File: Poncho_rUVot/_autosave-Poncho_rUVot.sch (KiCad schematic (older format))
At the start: 20 parts, among them J1 Screw_Terminal_01x03, K1 G5V-1, P10 Conn_01x04, P11 Conn_01x08, P3 Conn_01x03, P4 Conn_01x03, P5 Conn_01x04, P6 Conn_01x02, P7 Conn_01x02, P8 Conn_01x03, P9 Conn_01x06, Q1 BC548, Q2 BC548

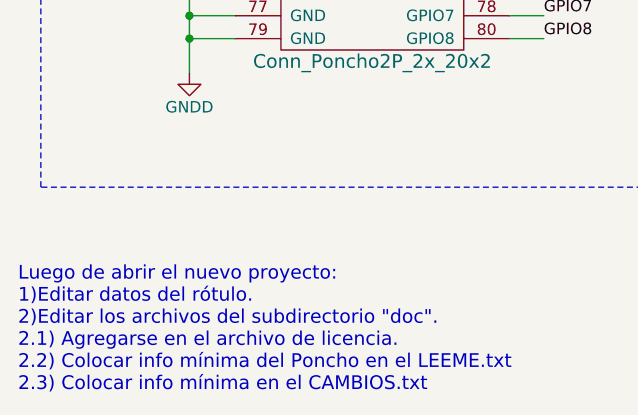
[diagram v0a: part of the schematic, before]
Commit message: Se acrualizan archivos carpeta DOC
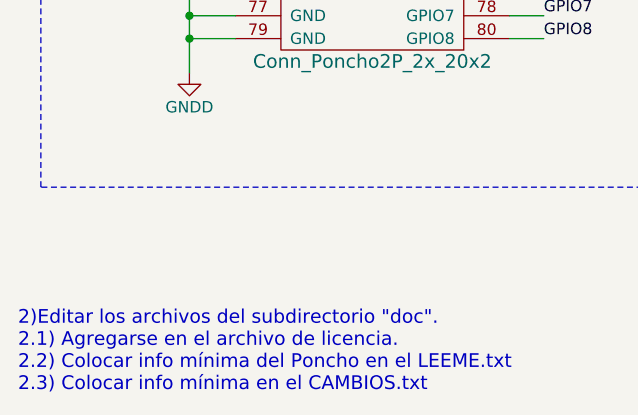
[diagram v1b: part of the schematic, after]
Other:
- note added: "\n2)Editar los archivos del subdirectorio "doc".\n2.1) Agregarse en el archivo de licencia.\n2.2) Colocar info mínima del Poncho en el LEEME.txt\n2.3) Colocar info mínima en el CAMBIOS.txt"
- note removed: "Luego de abrir el nuevo proyecto:\n1)Editar datos del rótulo.\n2)Editar los archivos del subdirectorio "doc".\n2.1) Agregarse en el archivo de licencia.\n2.2) Colocar info mínima del Poncho en el LEEME.txt\n2.3) Colocar info mínima en el CAMBIOS.txt"
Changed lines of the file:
@@
 encoding utf-8
 Sheet 1 1
-Title "Poncho Básico (Editar y colocar el nombre final)"
+Title "Poncho rUVot - Sergio Alberino"
 Date "2016-08-07"
 Rev "1.0"
 Comp "Proyecto CIAA - COMPUTADORA INDUSTRIAL ABIERTA ARGENTINA"
-Comment1 "https://github.com/ciaa/Ponchos/tree/master/Basico/doc"
+Comment1 "https://github.com/cese-dci/tp-SergioAlberino.git"
 Comment2 "Autores y Licencia del modelo (Diego Brengi - UNLaM)"
-Comment3 "Autor del poncho (COMPLETAR NOMBRE Y APELLIDO). Ver directorio \"doc\""
+Comment3 "Autor del poncho: sergio Alberino"
 Comment4 ""
 $EndDescr
@@
 	1    0    0    -1
 $EndComp
-Text Notes 650  7650 0    60   ~ 0
-Luego de abrir el nuevo proyecto:\n1)Editar datos del rótulo.\n2)Editar los archivos del subdirectorio "doc".\n2.1) Agregarse en el archivo de licencia.\n2.2) Colocar info mínima del Poncho en el LEEME.txt\n2.3) Colocar info mínima en el CAMBIOS.txt
 $Comp
 L Poncho_rUVot-rescue:GND #PWR06
@@
 Wire Notes Line
 	9050 2000 10950 2000
+Text Notes 650  7650 0    60   ~ 0
+\n2)Editar los archivos del subdirectorio "doc".\n2.1) Agregarse en el archivo de licencia.\n2.2) Colocar info mínima del Poncho en el LEEME.txt\n2.3) Colocar info mínima en el CAMBIOS.txt
 $EndSCHEMATC
